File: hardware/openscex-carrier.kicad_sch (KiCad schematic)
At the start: 20 parts, among them J1 ISP, Q1 2N3904, SW1 CTS 206-2ST, U1 ATtiny85-20PU

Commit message: feat(hardware): name datasheet-checked parts
Every BOM line now names an exact manufacturer part, each checked
against its own datasheet: Microchip ATTINY85-20PU in a TE
1-2199298-2 socket, KEMET C315C104K5R5TA, Panasonic EEU-FC1A101S,
Vishay MBA0204 resistors, onsemi 2N3904RLRAG and 1N4148TR,
Kingbright WP710A10ID, CTS 206-2ST, Same Sky CMI-1295IC-0385T and
Wurth 61200621621.

C1 moves to a 4.0 x 2.5 mm footprint that fits the KEMET body. A
project footprint library, hardware/openscex.pretty, carries the hole
sizes the Wurth header and the buzzer datasheets recommend, 1.1 mm and
0.8 mm in 2 mm pads.
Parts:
- BZ1: footprint Buzzer_Beeper:Buzzer_12x9.5RM7.6 -> openscex:Buzzer_12x9.5RM7.6_CMI-1295IC-0385T
- C1: footprint Capacitor_THT:C_Disc_D3.0mm_W1.6mm_P2.50mm -> Capacitor_THT:C_Rect_L4.0mm_W2.5mm_P2.50mm; Part 100 nF ceramic disc, 50 V, 2.5 mm pitch -> KEMET C315C104K5R5TA, 100 nF 50 V X7R, 2.54 mm
- C2: Part 100 uF 10 V radial electrolytic, 5 mm diameter, 2 mm pitch -> Panasonic EEU-FC1A101S, 100 uF 10 V, 105 C, 5 x 11 mm, 2.0 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
- D1: Part 3 mm red LED -> Kingbright WP710A10ID, 3 mm red LED
- D2: Part 1N4148, DO-35 -> onsemi 1N4148TR, DO-35
- J1: footprint Connector_IDC:IDC-Header_2x03_P2.54mm_Vertical -> openscex:IDC-Header_2x03_P2.54mm_Vertical_Wurth_61200621621; Part 2x3 shrouded box header, 2.54 mm, vertical -> Wurth 61200621621, 2x3 box header, 2.54 mm
- Q1: Part 2N3904 NPN, TO-92, legs formed to 2.54 mm -> onsemi 2N3904RLRAG, TO-92 with bent leads, 2.54 mm
- R1, R2: Part 1 kOhm axial resistor, DIN0204, 5.08 mm pitch -> Vishay MBA02040C1001FC100, 1 kOhm 1 % 0.4 W, 0204
- R3, R5: Part 10 kOhm axial resistor, DIN0204, 5.08 mm pitch -> Vishay MBA02040C1002FC100, 10 kOhm 1 % 0.4 W, 0204
- R4: Part 10 Ohm axial resistor, DIN0204, 5.08 mm pitch -> Vishay MBA02040C1009FC100, 10 Ohm 1 % 0.4 W, 0204
- U1: Part ATtiny85-20PU in a DIP-8 7.62 mm socket -> Microchip ATTINY85-20PU in a TE 1-2199298-2 DIP-8 socket
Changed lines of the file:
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@@
 	(property "Footprint" "Package_DIP:DIP-8_W7.62mm_Socket" (at 76.2 76.2 0) (effects (font (size 1.27 1.27)) (hide yes)))
 	(property "Datasheet" "" (at 76.2 76.2 0) (effects (font (size 1.27 1.27)) (hide yes)))
-	(property "Part" "ATtiny85-20PU in a DIP-8 7.62 mm socket" (at 76.2 76.2 0) (effects (font (size 1.27 1.27)) (hide yes)))
+	(property "Part" "Microchip ATTINY85-20PU in a TE 1-2199298-2 DIP-8 socket" (at 76.2 76.2 0) (effects (font (size 1.27 1.27)) (hide yes)))
 	(pin "1")
 	(pin "2")
@@
 	(property "Reference" "C1" (at 38.1 70.2 0) (effects (font (size 1.27 1.27))))
 	(property "Value" "100nF" (at 38.1 82.2 0) (effects (font (size 1.27 1.27))))
-	(property "Footprint" "Capacitor_THT:C_Disc_D3.0mm_W1.6mm_P2.50mm" (at 38.1 76.2 0) (effects (font (size 1.27 1.27)) (hide yes)))
+	(property "Footprint" "Capacitor_THT:C_Rect_L4.0mm_W2.5mm_P2.50mm" (at 38.1 76.2 0) (effects (font (size 1.27 1.27)) (hide yes)))
 	(property "Datasheet" "" (at 38.1 76.2 0) (effects (font (size 1.27 1.27)) (hide yes)))
-	(property "Part" "100 nF ceramic disc, 50 V, 2.5 mm pitch" (at 38.1 76.2 0) (effects (font (size 1.27 1.27)) (hide yes)))
+	(property "Part" "KEMET C315C104K5R5TA, 100 nF 50 V X7R, 2.54 mm" (at 38.1 76.2 0) (effects (font (size 1.27 1.27)) (hide yes)))
 	(pin "1")
 	(pin "2")
@@
 	(property "Footprint" "Resistor_THT:R_Axial_DIN0204_L3.6mm_D1.6mm_P5.08mm_Horizontal" (at 127.0 50.8 0) (effects (font (size 1.27 1.27)) (hide yes)))
 	(property "Datasheet" "" (at 127.0 50.8 0) (effects (font (size 1.27 1.27)) (hide yes)))
-	(property "Part" "1 kOhm axial resistor, DIN0204, 5.08 mm pitch" (at 127.0 50.8 0) (effects (font (size 1.27 1.27)) (hide yes)))
+	(property "Part" "Vishay MBA02040C1001FC100, 1 kOhm 1 % 0.4 W, 0204" (at 127.0 50.8 0) (effects (font (size 1.27 1.27)) (hide yes)))
 	(pin "1")
 	(pin "2")
@@
 	(property "Footprint" "Resistor_THT:R_Axial_DIN0204_L3.6mm_D1.6mm_P5.08mm_Horizontal" (at 142.24 50.8 0) (effects (font (size 1.27 1.27)) (hide yes)))
 	(property "Datasheet" "" (at 142.24 50.8 0) (effects (font (size 1.27 1.27)) (hide yes)))
-	(property "Part" "10 kOhm axial resistor, DIN0204, 5.08 mm pitch" (at 142.24 50.8 0) (effects (font (size 1.27 1.27)) (hide yes)))
+	(property "Part" "Vishay MBA02040C1002FC100, 10 kOhm 1 % 0.4 W, 0204" (at 142.24 50.8 0) (effects (font (size 1.27 1.27)) (hide yes)))
 	(pin "1")
 	(pin "2")
@@
 	(property "Footprint" "Package_TO_SOT_THT:TO-92_Inline_Wide" (at 157.48 76.2 0) (effects (font (size 1.27 1.27)) (hide yes)))
 	(property "Datasheet" "" (at 157.48 76.2 0) (effects (font (size 1.27 1.27)) (hide yes)))
-	(property "Part" "2N3904 NPN, TO-92, legs formed to 2.54 mm" (at 157.48 76.2 0) (effects (font (size 1.27 1.27)) (hide yes)))
+	(property "Part" "onsemi 2N3904RLRAG, TO-92 with bent leads, 2.54 mm" (at 157.48 76.2 0) (effects (font (size 1.27 1.27)) (hide yes)))
 	(pin "1")
 	(pin "2")
@@
 	(property "Footprint" "LED_THT:LED_D3.0mm" (at 213.36 50.8 0) (effects (font (size 1.27 1.27)) (hide yes)))
 	(property "Datasheet" "" (at 213.36 50.8 0) (effects (font (size 1.27 1.27)) (hide yes)))
-	(property "Part" "3 mm red LED" (at 213.36 50.8 0) (effects (font (size 1.27 1.27)) (hide yes)))
+	(property "Part" "Kingbright WP710A10ID, 3 mm red LED" (at 213.36 50.8 0) (effects (font (size 1.27 1.27)) (hide yes)))
 	(pin "1")
 	(pin "2")
@@
 	(property "Footprint" "Resistor_THT:R_Axial_DIN0204_L3.6mm_D1.6mm_P5.08mm_Horizontal" (at 228.6 50.8 0) (effects (font (size 1.27 1.27)) (hide yes)))
 	(property "Datasheet" "" (at 228.6 50.8 0) (effects (font (size 1.27 1.27)) (hide yes)))
-	(property "Part" "1 kOhm axial resistor, DIN0204, 5.08 mm pitch" (at 228.6 50.8 0) (effects (font (size 1.27 1.27)) (hide yes)))
+	(property "Part" "Vishay MBA02040C1001FC100, 1 kOhm 1 % 0.4 W, 0204" (at 228.6 50.8 0) (effects (font (size 1.27 1.27)) (hide yes)))
 	(pin "1")
 	(pin "2")
@@
 	(property "Reference" "BZ1" (at 213.36 95.6 0) (effects (font (size 1.27 1.27))))
 	(property "Value" "CMI-1295IC-0385T" (at 213.36 107.6 0) (effects (font (size 1.27 1.27))))
-	(property "Footprint" "Buzzer_Beeper:Buzzer_12x9.5RM7.6" (at 213.36 101.6 0) (effects (font (size 1.27 1.27)) (hide yes)))
+	(property "Footprint" "openscex:Buzzer_12x9.5RM7.6_CMI-1295IC-0385T" (at 213.36 101.6 0) (effects (font (size 1.27 1.27)) (hide yes)))
 	(property "Datasheet" "" (at 213.36 101.6 0) (effects (font (size 1.27 1.27)) (hide yes)))
 	(property "Part" "Same Sky CMI-1295IC-0385T magnetic buzzer, 12 mm" (at 213.36 101.6 0) (effects (font (size 1.27 1.27)) (hide yes)))
@@
 	(property "Footprint" "Diode_THT:D_DO-35_SOD27_P7.62mm_Horizontal" (at 233.68 101.6 0) (effects (font (size 1.27 1.27)) (hide yes)))
 	(property "Datasheet" "" (at 233.68 101.6 0) (effects (font (size 1.27 1.27)) (hide yes)))
-	(property "Part" "1N4148, DO-35" (at 233.68 101.6 0) (effects (font (size 1.27 1.27)) (hide yes)))
+	(property "Part" "onsemi 1N4148TR, DO-35" (at 233.68 101.6 0) (effects (font (size 1.27 1.27)) (hide yes)))
 	(pin "1")
 	(pin "2")
@@
 	(property "Footprint" "Resistor_THT:R_Axial_DIN0204_L3.6mm_D1.6mm_P5.08mm_Horizontal" (at 254.0 76.2 0) (effects (font (size 1.27 1.27)) (hide yes)))
 	(property "Datasheet" "" (at 254.0 76.2 0) (effects (font (size 1.27 1.27)) (hide yes)))
-	(property "Part" "10 Ohm axial resistor, DIN0204, 5.08 mm pitch" (at 254.0 76.2 0) (effects (font (size 1.27 1.27)) (hide yes)))
+	(property "Part" "Vishay MBA02040C1009FC100, 10 Ohm 1 % 0.4 W, 0204" (at 254.0 76.2 0) (effects (font (size 1.27 1.27)) (hide yes)))
 	(pin "1")
 	(pin "2")
@@
 	(property "Footprint" "Capacitor_THT:CP_Radial_D5.0mm_P2.00mm" (at 269.24 76.2 0) (effects (font (size 1.27 1.27)) (hide yes)))
 	(property "Datasheet" "" (at 269.24 76.2 0) (effects (font (size 1.27 1.27)) (hide yes)))
-	(property "Part" "100 uF 10 V radial electrolytic, 5 mm diameter, 2 mm pitch" (at 269.24 76.2 0) (effects (font (size 1.27 1.27)) (hide yes)))
+	(property "Part" "Panasonic EEU-FC1A101S, 100 uF 10 V, 105 C, 5 x 11 mm, 2.0 mm" (at 269.24 76.2 0) (effects (font (size 1.27 1.27)) (hide yes)))
 	(pin "1")
 	(pin "2")
@@
 	(property "Footprint" "Resistor_THT:R_Axial_DIN0204_L3.6mm_D1.6mm_P5.08mm_Horizontal" (at 50.8 50.8 0) (effects (font (size 1.27 1.27)) (hide yes)))
 	(property "Datasheet" "" (at 50.8 50.8 0) (effects (font (size 1.27 1.27)) (hide yes)))
-	(property "Part" "10 kOhm axial resistor, DIN0204, 5.08 mm pitch" (at 50.8 50.8 0) (effects (font (size 1.27 1.27)) (hide yes)))
+	(property "Part" "Vishay MBA02040C1002FC100, 10 kOhm 1 % 0.4 W, 0204" (at 50.8 50.8 0) (effects (font (size 1.27 1.27)) (hide yes)))
 	(pin "1")
 	(pin "2")
@@
 	(property "Reference" "J1" (at 284.48 70.2 0) (effects (font (size 1.27 1.27))))
 	(property "Value" "ISP" (at 284.48 82.2 0) (effects (font (size 1.27 1.27))))
-	(property "Footprint" "Connector_IDC:IDC-Header_2x03_P2.54mm_Vertical" (at 284.48 76.2 0) (effects (font (size 1.27 1.27)) (hide yes)))
+	(property "Footprint" "openscex:IDC-Header_2x03_P2.54mm_Vertical_Wurth_61200621621" (at 284.48 76.2 0) (effects (font (size 1.27 1.27)) (hide yes)))
 	(property "Datasheet" "" (at 284.48 76.2 0) (effects (font (size 1.27 1.27)) (hide yes)))
-	(property "Part" "2x3 shrouded box header, 2.54 mm, vertical" (at 284.48 76.2 0) (effects (font (size 1.27 1.27)) (hide yes)))
+	(property "Part" "Wurth 61200621621, 2x3 box header, 2.54 mm" (at 284.48 76.2 0) (effects (font (size 1.27 1.27)) (hide yes)))
 	(pin "1")
 	(pin "2")

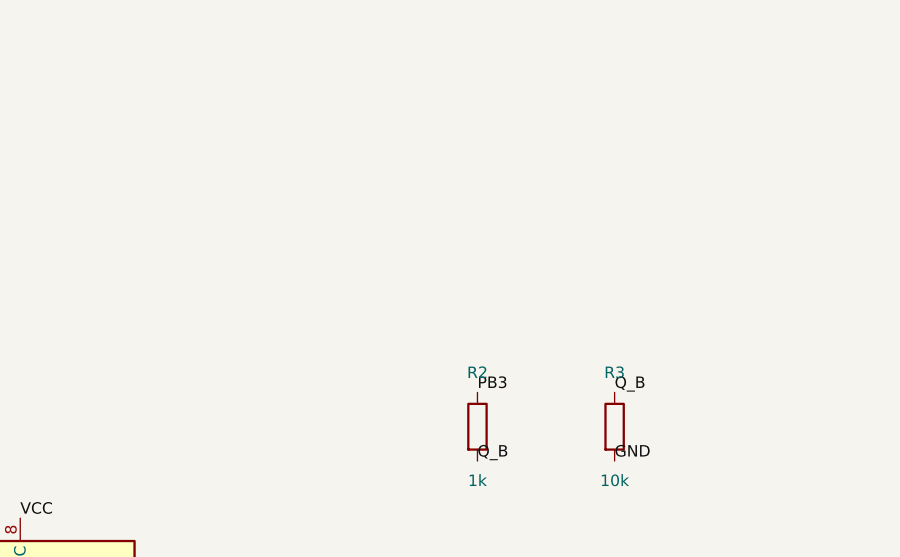
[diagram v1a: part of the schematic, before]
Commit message: feat(hardware): add a serial trace header
The carrier gains a band along its top edge for the trace profile: J2,
a 1x6 header in the FTDI TTL-232R pinout with only GND and the cable's
RXD wired, a C&K OS102011MS2QN1 slide switch that hands PB3 to the
indicator or to the header, and 1 kOhm in series with the serial line.
The lower board keeps the mini and bare layout and width.

C1's 3D model is scaled to the KEMET C315 body on all three boards; the
library model is a 10 mm film box.

The READMEs no longer say fat boards run at about 5 V: every board runs
its logic from +3.5 V, and the 5 V rail is not a chip supply.
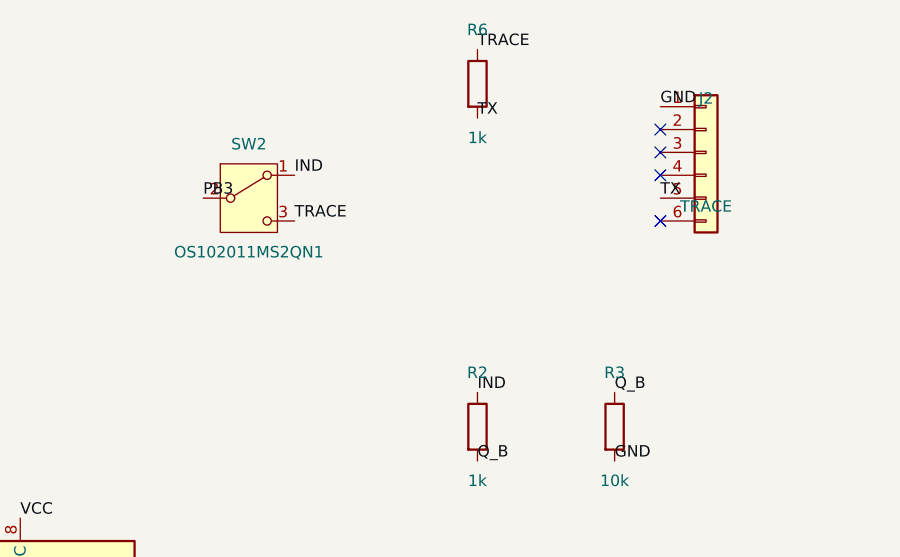
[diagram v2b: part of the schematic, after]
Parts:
- added J2: TRACE, Connector_PinHeader_2.54mm:PinHeader_1x06_P2.54mm_Vertical, symbol Connector_Generic:Conn_01x06
- added R6: 1k, Resistor_THT:R_Axial_DIN0204_L3.6mm_D1.6mm_P5.08mm_Horizontal, symbol Device:R
- added SW2: OS102011MS2QN1, openscex:SW_Slide_SPDT_Straight_CK_OS102011MS2Q, symbol Switch:SW_SPDT
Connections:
- net GND: now also J2.1 (Pin_1)
- net PB3: now also SW2.2 (B); no longer R2.1
- new net IND: R2.1, SW2.1 (A)
- new net TRACE: R6.1, SW2.3 (C)
- new net TX: J2.5 (Pin_5), R6.2
- no-connect marks 0 -> 4
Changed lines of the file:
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@@
 (kicad_sch (version 20231120) (generator "eeschema") (generator_version "8.0")
 	(paper "A3")
-	(title_block (title "openscex carrier") (comment 1 "ATtiny85 PS1 modchip carrier: socket, decoupling, LED or buzzer indicator through Q1"))
+	(title_block (title "openscex carrier") (comment 1 "ATtiny85 PS1 modchip carrier: socket, decoupling, LED or buzzer indicator through Q1, serial trace header"))
 (symbol (lib_id "MCU_Microchip_ATtiny:ATtiny85-20P") (at 76.2 76.2 0) (unit 1)
 	(in_bom yes) (on_board yes) (dnp no)
@@
 	(instances (project "openscex-carrier" (path "/7206801e-1c20-5311-8a84-3899543930cc" (reference "R2") (unit 1))))
 )
-(label "PB3" (at 127.0 46.99 0) (effects (font (size 1.27 1.27)) (justify left bottom)))
+(label "IND" (at 127.0 46.99 0) (effects (font (size 1.27 1.27)) (justify left bottom)))
 (label "Q_B" (at 127.0 54.61 0) (effects (font (size 1.27 1.27)) (justify left bottom)))
 (symbol (lib_id "Device:R") (at 142.24 50.8 0) (unit 1)
@@
 (label "RST" (at 279.4 78.74 0) (effects (font (size 1.27 1.27)) (justify left bottom)))
 (label "GND" (at 292.1 78.74 0) (effects (font (size 1.27 1.27)) (justify left bottom)))
+(symbol (lib_id "Switch:SW_SPDT") (at 101.6 25.4 0) (unit 1)
+	(in_bom yes) (on_board yes) (dnp no)
+	(property "Reference" "SW2" (at 101.6 19.4 0) (effects (font (size 1.27 1.27))))
+	(property "Value" "OS102011MS2QN1" (at 101.6 31.4 0) (effects (font (size 1.27 1.27))))
+	(property "Footprint" "openscex:SW_Slide_SPDT_Straight_CK_OS102011MS2Q" (at 101.6 25.4 0) (effects (font (size 1.27 1.27)) (hide yes)))
+	(property "Datasheet" "" (at 101.6 25.4 0) (effects (font (size 1.27 1.27)) (hide yes)))
+	(property "Part" "C&K OS102011MS2QN1, SPDT slide switch, 2.00 mm" (at 101.6 25.4 0) (effects (font (size 1.27 1.27)) (hide yes)))
+	(pin "1")
+	(pin "2")
+	(pin "3")
+	(instances (project "openscex-carrier" (path "/7206801e-1c20-5311-8a84-3899543930cc" (reference "SW2") (unit 1))))
+)
+(label "IND" (at 106.68 22.86 0) (effects (font (size 1.27 1.27)) (justify left bottom)))
+(label "PB3" (at 96.52 25.4 0) (effects (font (size 1.27 1.27)) (justify left bottom)))
+(label "TRACE" (at 106.68 27.94 0) (effects (font (size 1.27 1.27)) (justify left bottom)))
+(symbol (lib_id "Device:R") (at 127.0 12.7 0) (unit 1)
+	(in_bom yes) (on_board yes) (dnp no)
+	(property "Reference" "R6" (at 127.0 6.699999999999999 0) (effects (font (size 1.27 1.27))))
+	(property "Value" "1k" (at 127.0 18.7 0) (effects (font (size 1.27 1.27))))
+	(property "Footprint" "Resistor_THT:R_Axial_DIN0204_L3.6mm_D1.6mm_P5.08mm_Horizontal" (at 127.0 12.7 0) (effects (font (size 1.27 1.27)) (hide yes)))
+	(property "Datasheet" "" (at 127.0 12.7 0) (effects (font (size 1.27 1.27)) (hide yes)))
+	(property "Part" "Vishay MBA02040C1001FC100, 1 kOhm 1 % 0.4 W, 0204" (at 127.0 12.7 0) (effects (font (size 1.27 1.27)) (hide yes)))
+	(pin "1")
+	(pin "2")
+	(instances (project "openscex-carrier" (path "/7206801e-1c20-5311-8a84-3899543930cc" (reference "R6") (unit 1))))
+)
+(label "TRACE" (at 127.0 8.89 0) (effects (font (size 1.27 1.27)) (justify left bottom)))
+(label "TX" (at 127.0 16.51 0) (effects (font (size 1.27 1.27)) (justify left bottom)))
+(symbol (lib_id "Connector_Generic:Conn_01x06") (at 152.4 20.32 0) (unit 1)
+	(in_bom yes) (on_board yes) (dnp no)
+	(property "Reference" "J2" (at 152.4 14.32 0) (effects (font (size 1.27 1.27))))
+	(property "Value" "TRACE" (at 152.4 26.32 0) (effects (font (size 1.27 1.27))))
+	(property "Footprint" "Connector_PinHeader_2.54mm:PinHeader_1x06_P2.54mm_Vertical" (at 152.4 20.32 0) (effects (font (size 1.27 1.27)) (hide yes)))
+	(property "Datasheet" "" (at 152.4 20.32 0) (effects (font (size 1.27 1.27)) (hide yes)))
+	(property "Part" "Wurth 61300611121, 1x6 pin header, 2.54 mm" (at 152.4 20.32 0) (effects (font (size 1.27 1.27)) (hide yes)))
+	(pin "1")
+	(pin "2")
+	(pin "3")
+	(pin "4")
+	(pin "5")
+	(pin "6")
+	(instances (project "openscex-carrier" (path "/7206801e-1c20-5311-8a84-3899543930cc" (reference "J2") (unit 1))))
+)
+(label "GND" (at 147.32 15.24 0) (effects (font (size 1.27 1.27)) (justify left bottom)))
+(no_connect (at 147.32 17.78))
+(no_connect (at 147.32 20.32))
+(no_connect (at 147.32 22.86))
+(label "TX" (at 147.32 25.4 0) (effects (font (size 1.27 1.27)) (justify left bottom)))
+(no_connect (at 147.32 27.94))
 (symbol (lib_id "Connector:TestPoint") (at 50.8 139.7 0) (unit 1)
 	(in_bom no) (on_board yes) (dnp no)
